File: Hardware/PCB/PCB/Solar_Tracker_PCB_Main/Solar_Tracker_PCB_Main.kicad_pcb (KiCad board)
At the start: 4 copper layers, 95.4 x 96.8 mm, 59 parts, among them IC1 ESP32-S3-WROOM-1-N4R8, IC2 TPS54302DDCT, IC3 BNO085, IC4 PCF2131TFY, IC5 LM1117MPX-3.3_NOPB, J1 1729076, J2 USB4940-00-A, J3 1729076, J4 1977223-1, J5 1977223-1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

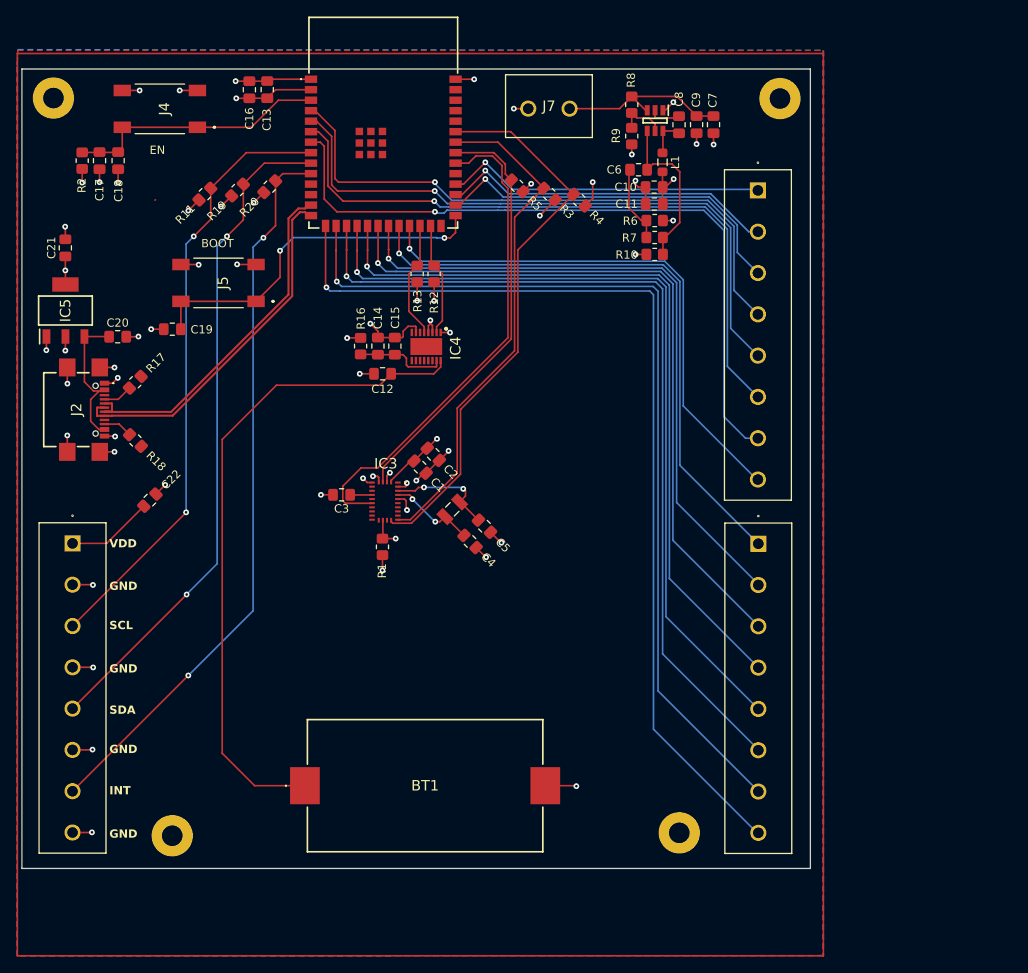
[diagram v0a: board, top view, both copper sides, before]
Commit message: Agregue vias GND cerca de las vias VDD
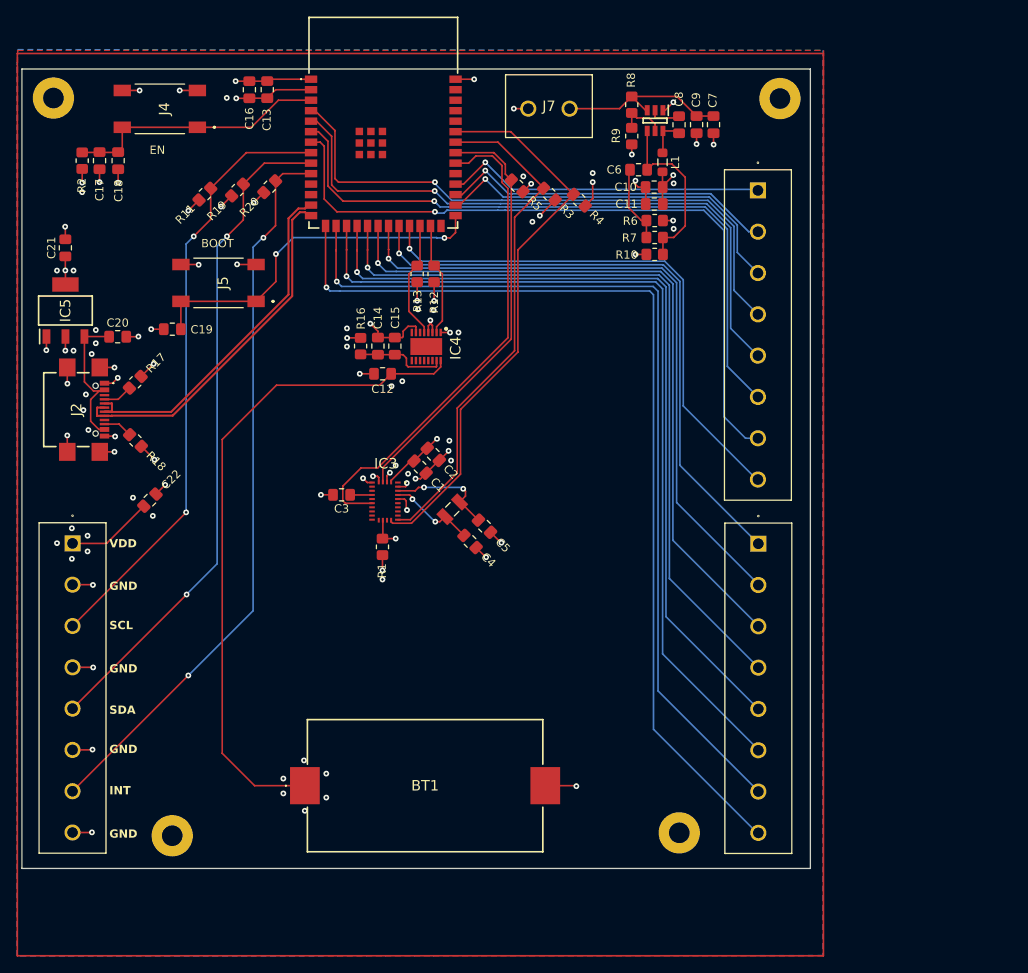
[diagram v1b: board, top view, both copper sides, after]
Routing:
- net GND: track 103.7 -> 108.1 mm, vias 42 -> 85
- net Net-(IC2-FB): track 20.3 -> 21.5 mm

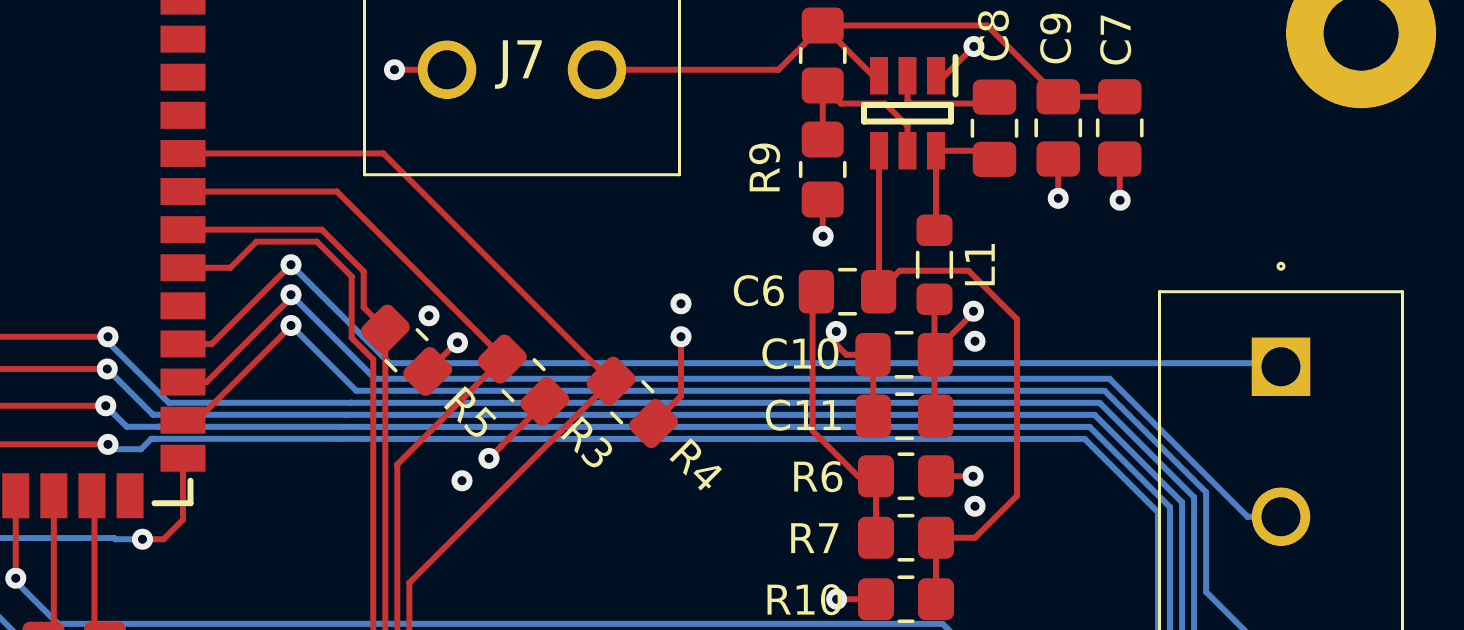
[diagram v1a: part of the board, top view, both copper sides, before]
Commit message: Agregar tierra a las Borneras
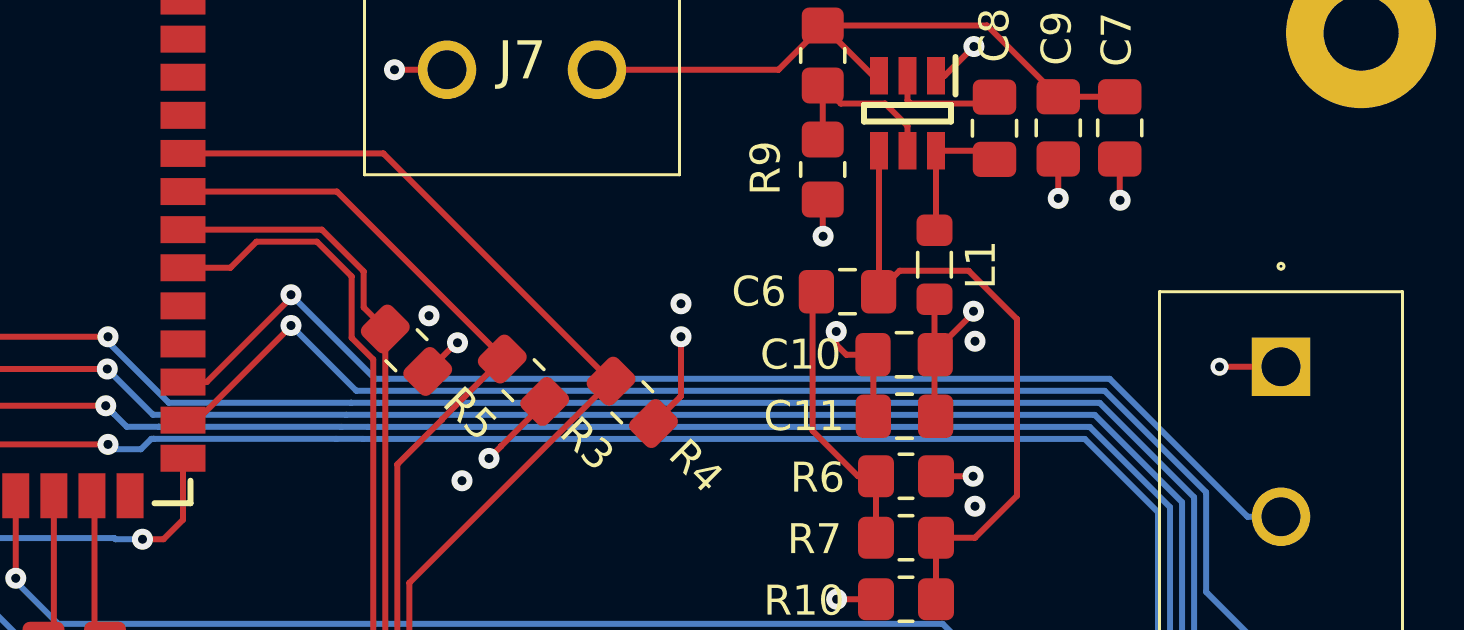
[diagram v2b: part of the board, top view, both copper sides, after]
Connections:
- IC1 pad 30: J6_1 -> unconnected-(IC1-IO37-Pad30)
- J6 pad 1: J6_1 -> GND
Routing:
- net J6_1: track 39.1 -> 0.00 mm, vias 1 -> 0
- net GND: track 108.1 -> 110.1 mm, vias 85 -> 86

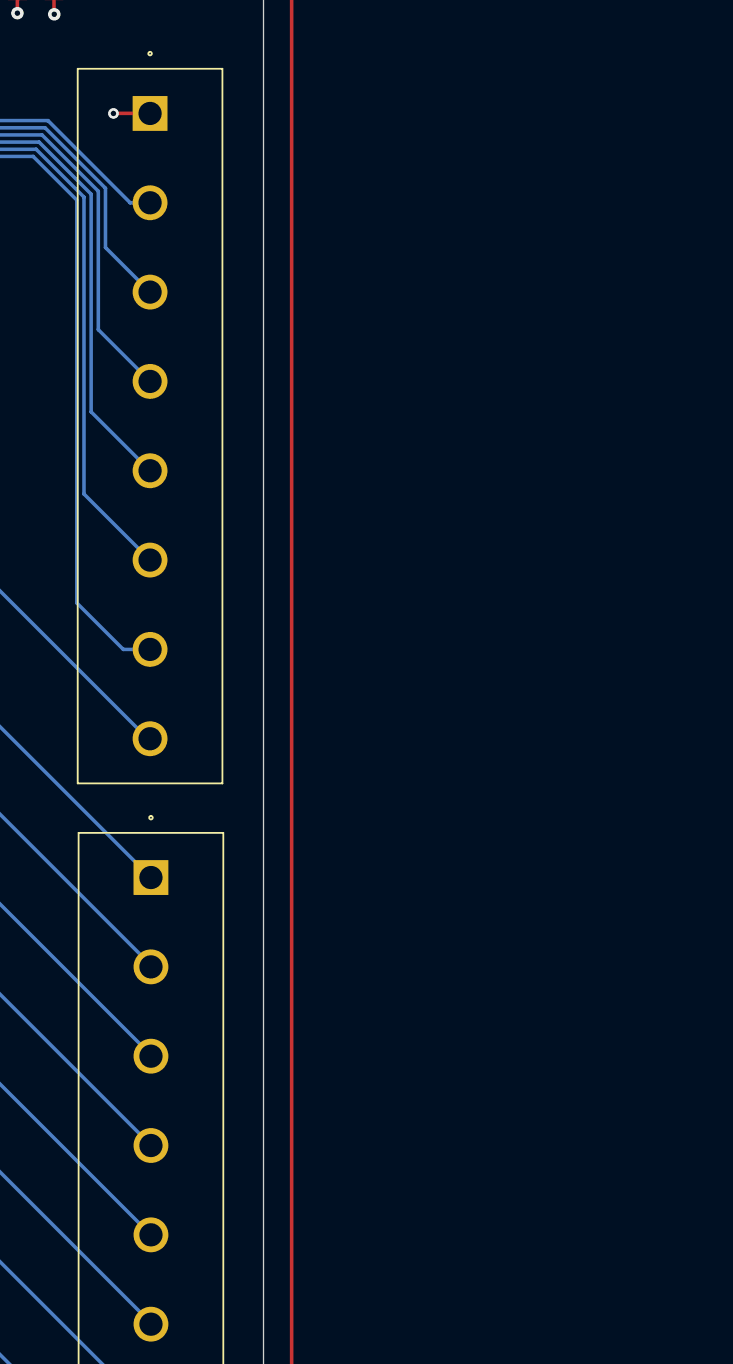
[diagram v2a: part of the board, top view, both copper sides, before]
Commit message: Nuevo conector JST
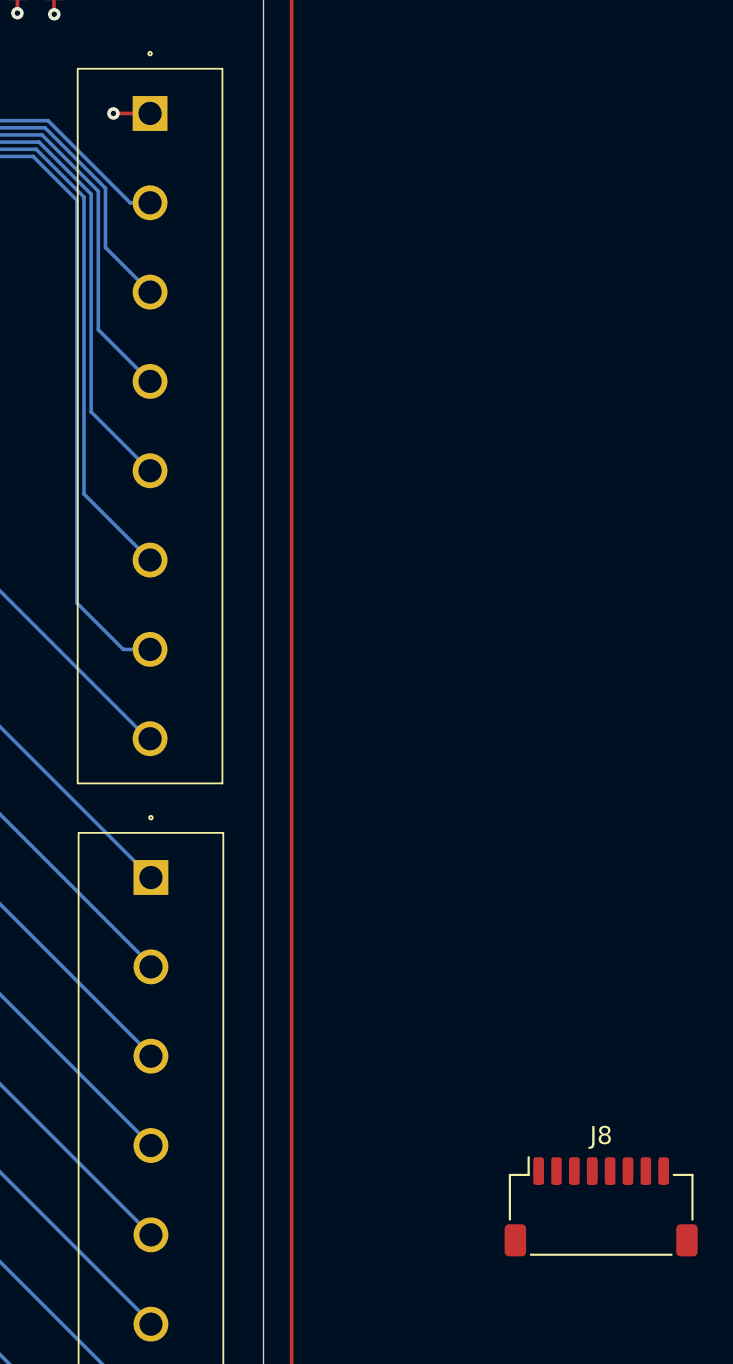
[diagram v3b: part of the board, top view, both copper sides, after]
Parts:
- added J8: Conn_01x08_Pin, Connector_JST:JST_SH_SM08B-SRSS-TB_1x08-1MP_P1.00mm_Horizontal, F.Cu at (185.1, 120.4)
